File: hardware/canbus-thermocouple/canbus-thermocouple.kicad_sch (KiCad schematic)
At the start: 33 parts, among them J1 USB_B_Micro, J2 UART, J3 10k NTC, J4 CANBus, J5 CANBus, J6 SWD, Q1 2N7002, Q2 2N7002, U1 MCP1754S-3302xCB, U2 STM32F042F6Px, U3 Voltage Regulator, U4 MCP2562HD

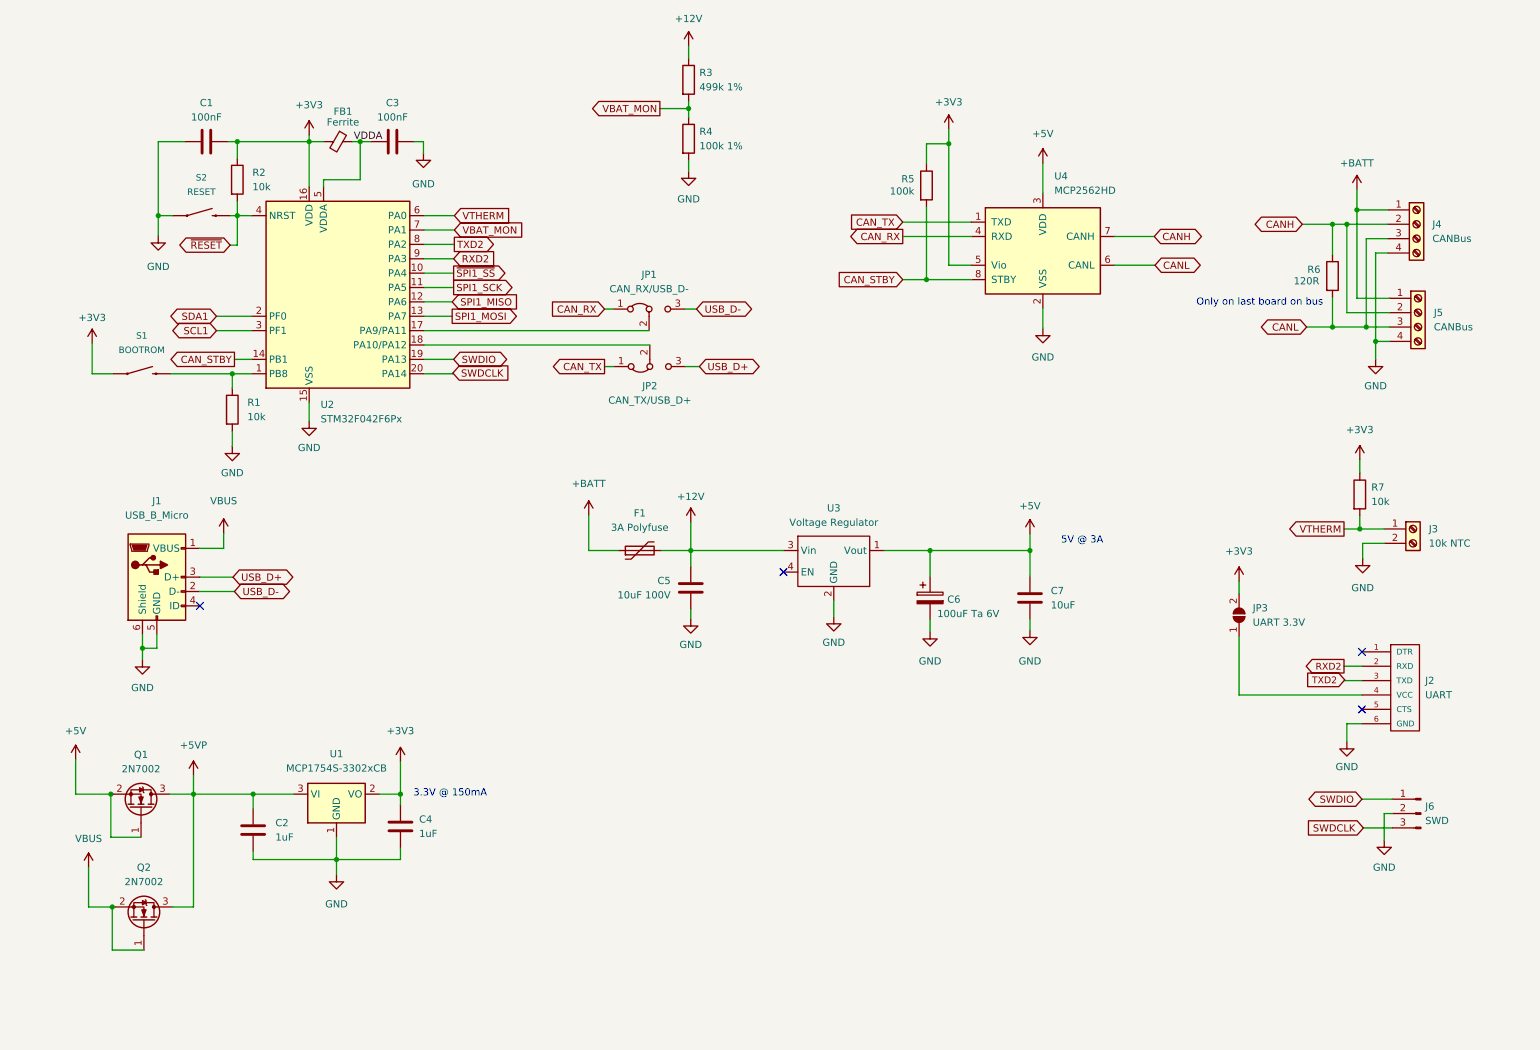
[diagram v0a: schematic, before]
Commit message: Updated the thermocouple board, added OSHW to bottom of all boards
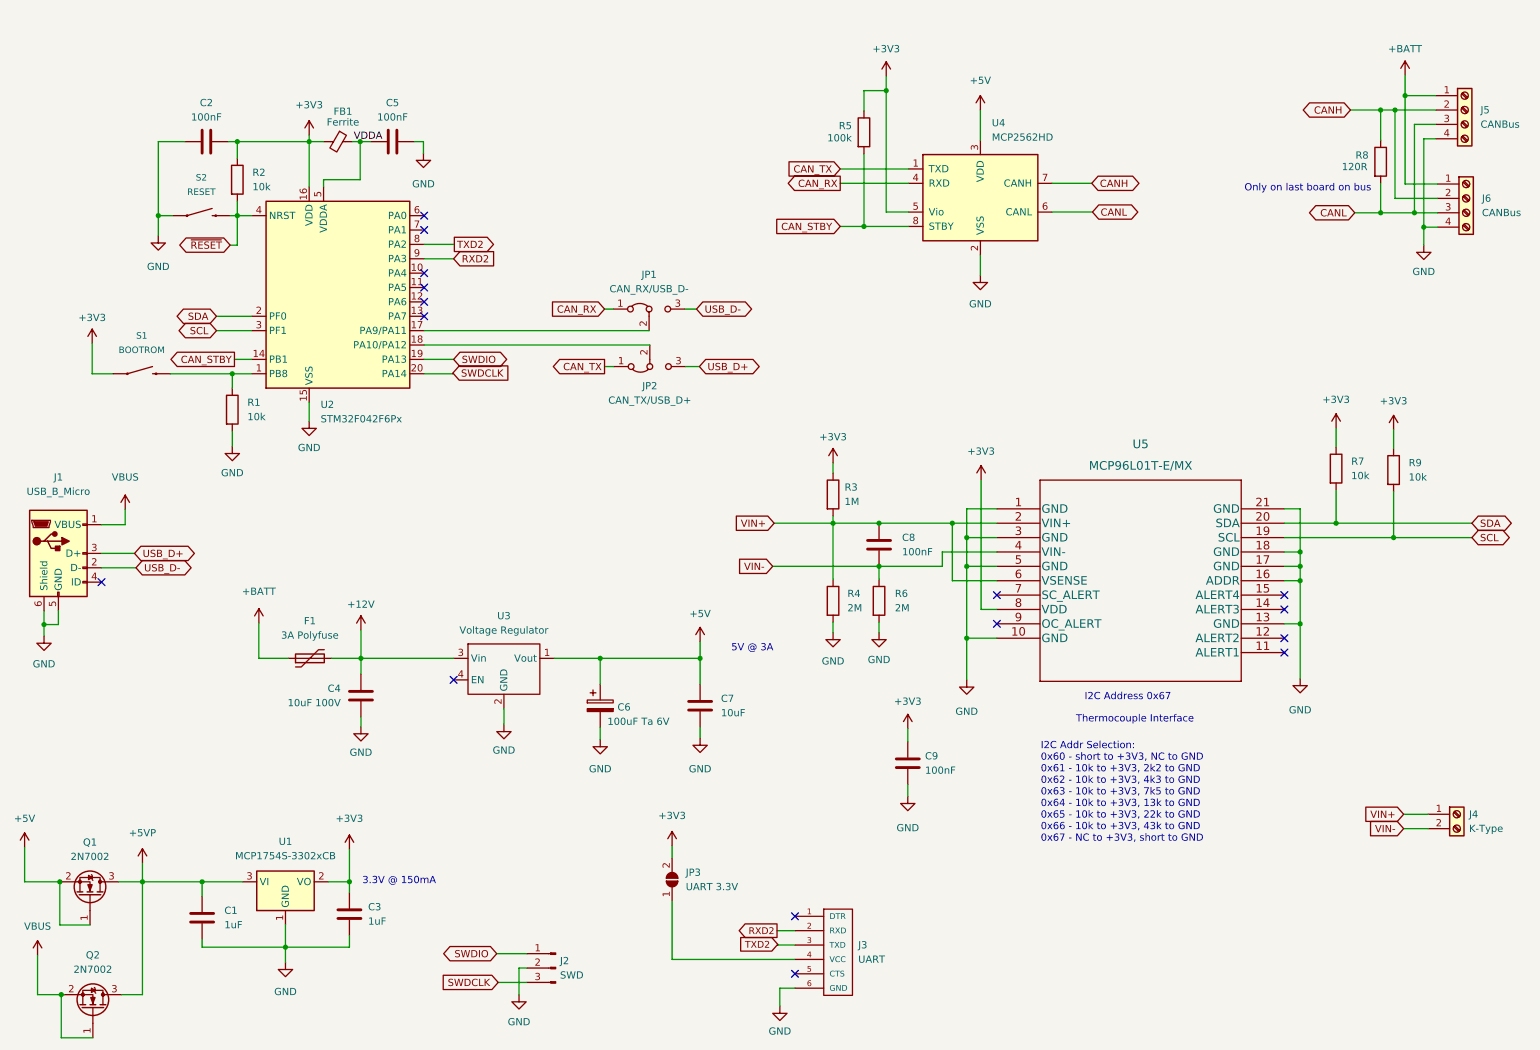
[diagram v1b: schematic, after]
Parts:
- removed J3: 10k NTC, TerminalBlock_TE-Connectivity:TerminalBlock_TE_282834-2_1x02_P2.54mm_Horizontal, symbol Connector:Screw_Terminal_01x02
- added C8, C9: 100nF, Capacitor_SMD:C_0805_2012Metric_Pad1.18x1.45mm_HandSolder, symbol Device:C
- added J4: K-Type, TerminalBlock_TE-Connectivity:TerminalBlock_TE_282834-2_1x02_P2.54mm_Horizontal, symbol Connector:Screw_Terminal_01x02
- added R6: 2M, Resistor_SMD:R_0805_2012Metric_Pad1.20x1.40mm_HandSolder, symbol Device:R
- added R9: 10k, Resistor_SMD:R_0805_2012Metric_Pad1.20x1.40mm_HandSolder, symbol Device:R
- added U5: MCP96L01T-E/MX, UltraLibrarian:MCP96L01T-E&slash_MX, symbol UltraLibrarian:MCP96L01T-E{brace}slash}MX
- JP3: footprint (none) -> Jumper:SolderJumper-2_P1.3mm_Open_TrianglePad1.0x1.5mm
- R3: value 499k 1% -> 1M
- R4: value 100k 1% -> 2M
- renumbered C2 to C1, C1 to C2, C4 to C3, C5 to C4, C3 to C5, J6 to J2, J2 to J3, J4 to J5, J5 to J6, R6 to R8
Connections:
- net +12V: no longer R3.1
- net +3V3: now also R3.1, C9.1, R9.1, U5.8 (VDD)
- net GND: now also C9.2, R6.2, U5.1 (GND), U5.10 (GND), U5.13 (GND), U5.16 (ADDR), U5.17 (GND), U5.18 (GND), U5.21 (GND), U5.3 (GND), U5.5 (GND)
- net SCL1 renamed SCL
- net SCL: now also R9.2, U5.19 (SCL)
- net SDA1 renamed SDA
- net SDA: now also R7.2, U5.20 (SDA)
- net SPI1_MISO: no longer names the net of U2.12 (PA6)
- net SPI1_MOSI: no longer names the net of U2.13 (PA7)
- net SPI1_SCK: no longer names the net of U2.11 (PA5)
- net VBAT_MON renamed VIN+
- net VIN+: now also C8.1, J4.1 (Pin_1), U5.2 (VIN+), U5.6 (VSENSE); no longer U2.7 (PA1)
- net VTHERM: no longer names the net of U2.6 (PA0)
- net VTHERM: no longer R7.2
- net ~{SPI1_SS}: no longer names the net of U2.10 (PA4)
- new net VIN-: C8.2, J4.2 (Pin_2), R6.1, U5.4 (VIN-)
- no-connect marks 4 -> 16
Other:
- note added: "I2C Addr Selection: 0x60 - short to +3V3, NC to GND 0x61 - 10k to +3V3, 2k2 to GND 0x62 - 10k to +3V3, 4k3 to GND 0x63 - 10k to +3V3, 7k5 to GND 0x64 - 10k to +3V3, 13k to GND 0x65 - 10k to +3V3, 22k to GND 0x66 - 10k to +3V3, 43k to GND 0x67 - NC to +3V3, short to GND"
- note added: "I2C Address 0x67"
- note added: "Thermocouple Interface"
- title: CANBus Thermistor Sensor -> CANBus Thermocouple Sensor
- moved on the sheet: C1, C3, C4, C6, C7, F1, J1, J2, J3, J5, J6, JP3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
